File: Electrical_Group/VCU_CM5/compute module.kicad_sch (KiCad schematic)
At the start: 8 parts

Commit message: [VCU_CM5] update to V1.2
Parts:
- Module1: footprint CM5IO:Raspberry-Pi-5-Compute-Module -> nturt_kicad_lib_EP7:Raspberry-Pi-5-Compute-Module
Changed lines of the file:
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@@
 	(generator "eeschema")
 	(generator_version "9.0")
-	(paper "A4")
+	(paper "A3")
 	(title_block
 		(title "VCU_CM5")
 		(date "2026-02-25")
-		(rev "1.1")
+		(rev "1.2")
 		(company "NTURacing Team")
 		(comment 1 "Jack Kuo")
@@
 			)
 		)
-		(property "Footprint" "CM5IO:Raspberry-Pi-5-Compute-Module"
+		(property "Footprint" "nturt_kicad_lib_EP7:Raspberry-Pi-5-Compute-Module"
 			(at 218.44 114.3 0)
 			(effects
@@
 			)
 		)
-		(property "Footprint" "CM5IO:Raspberry-Pi-5-Compute-Module"
+		(property "Footprint" "nturt_kicad_lib_EP7:Raspberry-Pi-5-Compute-Module"
 			(at 227.33 109.22 0)
 			(effects

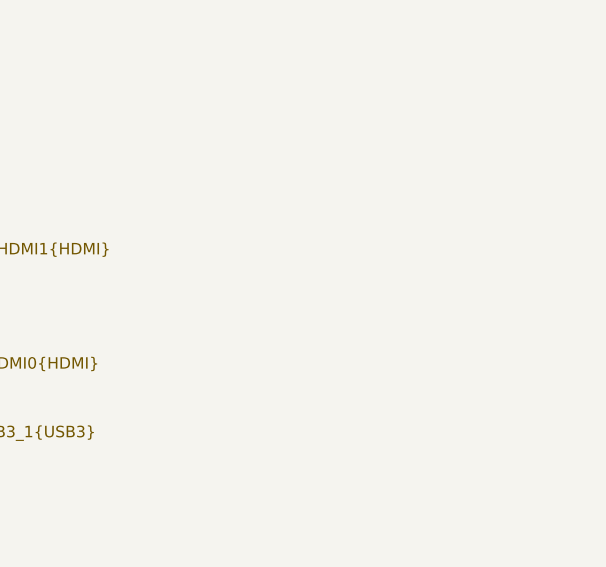
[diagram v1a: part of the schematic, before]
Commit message: [VCU_CM5] update to V1.3
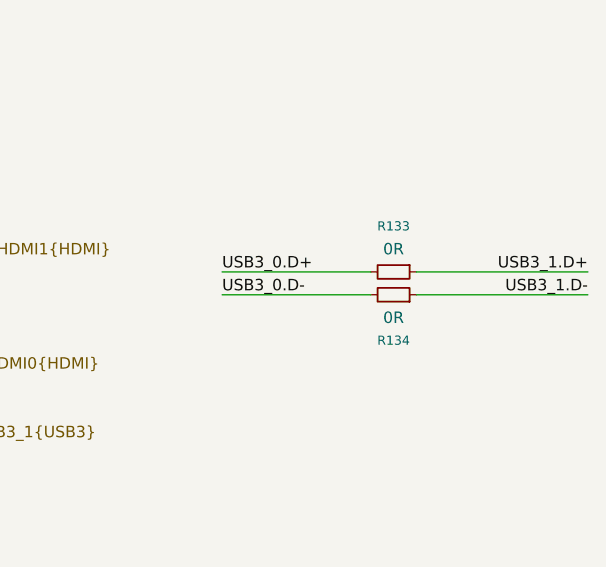
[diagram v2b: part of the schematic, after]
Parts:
- added R133, R134: 0R, Resistor_SMD:R_0603_1608Metric_Pad0.98x0.95mm_HandSolder, symbol Device:R_Small
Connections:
- net USB3_0.D+: now also R133.2
- net USB3_0.D-: now also R134.2
- net USB3_1.D+: now also R133.1
- net USB3_1.D-: now also R134.1
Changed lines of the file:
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@@
 	(title_block
 		(title "VCU_CM5")
-		(date "2026-02-25")
-		(rev "1.2")
+		(date "2026-02-28")
+		(rev "1.3")
 		(company "NTURacing Team")
 		(comment 1 "Jack Kuo")
@@
 	(wire
 		(pts
+			(xy 298.45 77.47) (xy 314.96 77.47)
+		)
+		(stroke
+			(width 0)
+			(type default)
+		)
+	)
+	(wire
+		(pts
 			(xy 247.65 140.97) (xy 247.65 148.59)
 		)
@@
 	(wire
 		(pts
+			(xy 298.45 80.01) (xy 314.96 80.01)
+		)
+		(stroke
+			(width 0)
+			(type default)
+		)
+	)
+	(wire
+		(pts
 			(xy 246.38 74.93) (xy 265.43 74.93)
 		)
@@
 		)
 	)
+	(wire
+		(pts
+			(xy 320.04 77.47) (xy 339.09 77.47)
+		)
+		(stroke
+			(width 0)
+			(type default)
+		)
+	)
 	(bus
 		(pts
@@
 	(wire
 		(pts
+			(xy 320.04 80.01) (xy 339.09 80.01)
+		)
+		(stroke
+			(width 0)
+			(type default)
+		)
+	)
+	(wire
+		(pts
 			(xy 265.43 105.41) (xy 246.38 105.41)
 		)
@@
 		)
 	)
+	(label "USB3_0.D-"
+		(at 298.45 80.01 0)
+		(effects
+			(font
+				(size 1.27 1.27)
+			)
+			(justify left bottom)
+		)
+	)
 	(label "SD.D2"
 		(at 115.57 113.03 0)
@@
 		)
 	)
+	(label "USB3_0.D+"
+		(at 298.45 77.47 0)
+		(effects
+			(font
+				(size 1.27 1.27)
+			)
+			(justify left bottom)
+		)
+	)
 	(label "USB3_0.D-"
 		(at 182.88 69.85 180)
@@
 		)
 	)
+	(label "USB3_1.D+"
+		(at 339.09 77.47 180)
+		(effects
+			(font
+				(size 1.27 1.27)
+			)
+			(justify right bottom)
+		)
+	)
 	(label "40P.GPIO5"
 		(at 49.53 67.31 180)
@@
 		)
 	)
+	(label "USB3_1.D-"
+		(at 339.09 80.01 180)
+		(effects
+			(font
+				(size 1.27 1.27)
+			)
+			(justify right bottom)
+		)
+	)
 	(label "SD.D3"
 		(at 115.57 102.87 0)
@@
 	(symbol
 		(lib_id "Device:R_Small")
+		(at 317.5 77.47 270)
+		(unit 1)
+		(exclude_from_sim no)
+		(in_bom yes)
+		(on_board yes)
+		(dnp no)
+		(fields_autoplaced yes)
+		(property "Reference" "R133"
+			(at 317.5 72.39 90)
+			(effects
+				(font
+					(size 1.016 1.016)
+				)
+			)
+		)
+		(property "Value" "0R"
+			(at 317.5 74.93 90)
+			(effects
+				(font
+					(size 1.27 1.27)
+				)
+			)
+		)
+		(property "Footprint" "Resistor_SMD:R_0603_1608Metric_Pad0.98x0.95mm_HandSolder"
+			(at 317.5 77.47 0)
+			(effects
+				(font
+					(size 1.27 1.27)
+				)
+				(hide yes)
+			)
+		)
+		(property "Datasheet" "~"
+			(at 317.5 77.47 0)
+			(effects
+				(font
+					(size 1.27 1.27)
+				)
+				(hide yes)
+			)
+		)
+		(property "Description" "Resistor, small symbol"
+			(at 317.5 77.47 0)
+			(effects
+				(font
+					(size 1.27 1.27)
+				)
+				(hide yes)
+			)
+		)
+		(pin "2"
+		)
+		(pin "1"
+		)
+		(instances
+			(project "VCU_CM5"
+				(path "/eb296f24-894e-4ea0-b0cd-3ba211155378/0b024046-a452-472c-8933-8dd8af0d7b70/0fe8afc8-b7c5-49f3-8318-2bf5095c7824"
+					(reference "R133")
+					(unit 1)
+				)
+			)
+		)
+	)
+	(symbol
+		(lib_id "Device:R_Small")
 		(at 43.18 49.53 90)
 		(unit 1)
@@
 					(unit 1)
 				)
+			)
+		)
+	)
+	(symbol
+		(lib_id "Device:R_Small")
+		(at 317.5 80.01 270)
+		(mirror x)
+		(unit 1)
+		(exclude_from_sim no)
+		(in_bom yes)
+		(on_board yes)
+		(dnp no)
+		(property "Reference" "R134"
+			(at 317.5 85.09 90)
+			(effects
+				(font
+					(size 1.016 1.016)
+				)
+			)
+		)
+		(property "Value" "0R"
+			(at 317.5 82.55 90)
+			(effects
+				(font
+					(size 1.27 1.27)
+				)
+			)
+		)
+		(property "Footprint" "Resistor_SMD:R_0603_1608Metric_Pad0.98x0.95mm_HandSolder"
+			(at 317.5 80.01 0)
+			(effects
+				(font
+					(size 1.27 1.27)
+				)
+				(hide yes)
+			)
+		)
+		(property "Datasheet" "~"
+			(at 317.5 80.01 0)
+			(effects
+				(font
+					(size 1.27 1.27)
+				)
+				(hide yes)
+			)
+		)
+		(property "Description" "Resistor, small symbol"
+			(at 317.5 80.01 0)
+			(effects
+				(font
+					(size 1.27 1.27)
+				)
+				(hide yes)
+			)
+		)
+		(pin "2"
+		)
+		(pin "1"
+		)
+		(instances
+			(project "VCU_CM5"
+				(path "/eb296f24-894e-4ea0-b0cd-3ba211155378/0b024046-a452-472c-8933-8dd8af0d7b70/0fe8afc8-b7c5-49f3-8318-2bf5095c7824"
+					(reference "R134")
+					(unit 1)
+				)
